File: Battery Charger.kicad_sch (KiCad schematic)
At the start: 2 parts, among them Q9 2SJ174, U16 CN3703

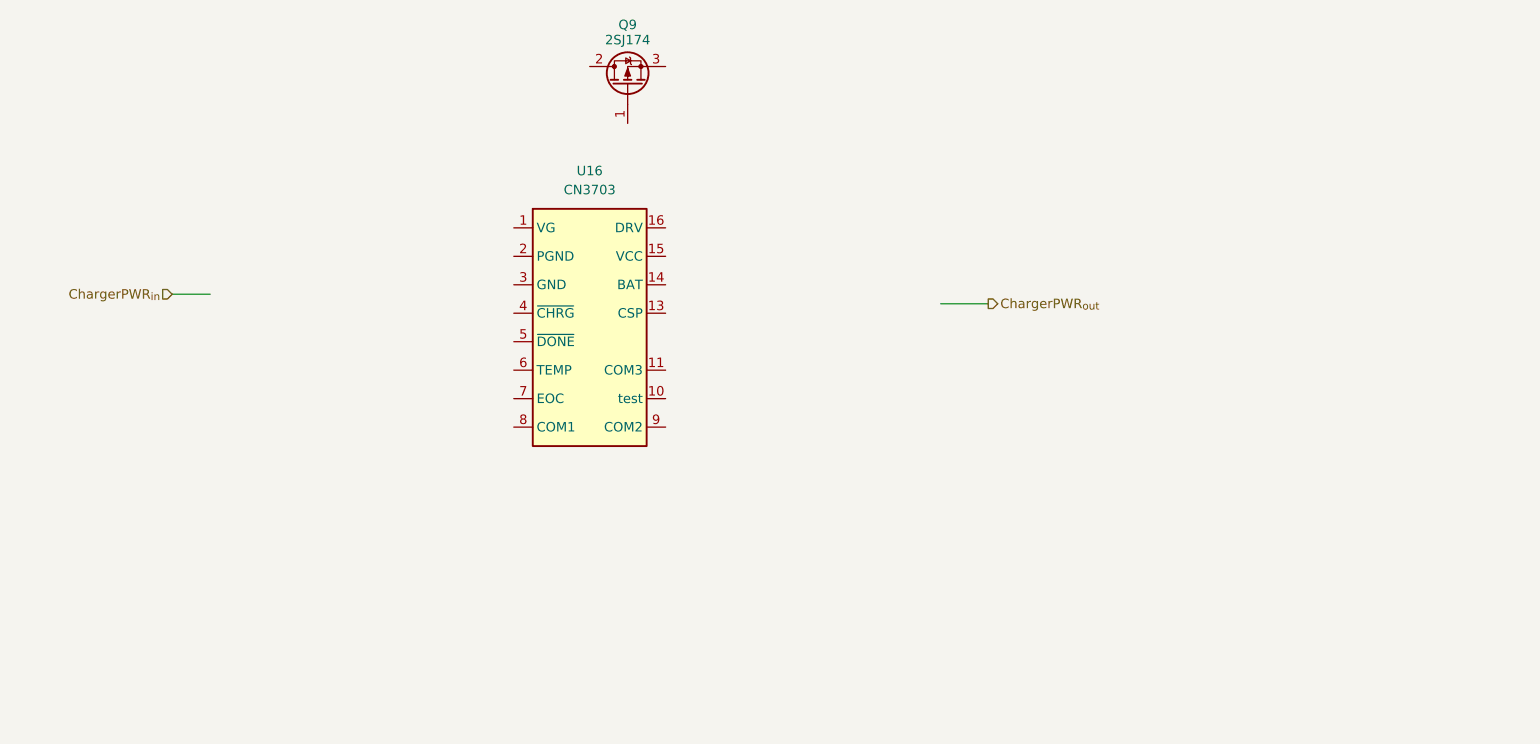
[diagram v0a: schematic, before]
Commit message: feat: Battery charging Circuit is added.
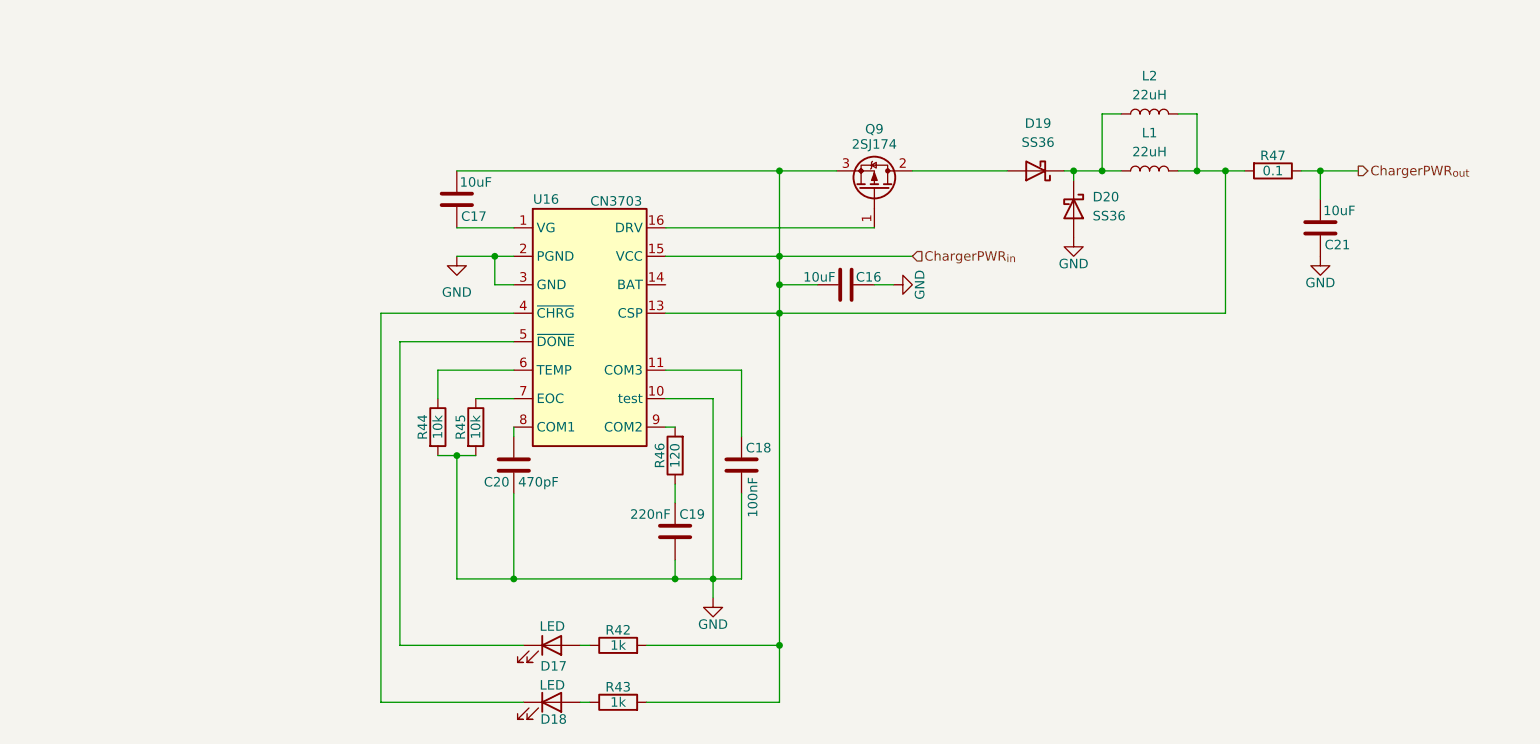
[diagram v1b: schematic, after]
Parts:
- added C16, C17, C21: 10uF, Capacitor_THT:C_Radial_D5.0mm_H5.0mm_P2.00mm, symbol Device:C
- added C18: 100nF, Capacitor_THT:C_Disc_D3.0mm_W2.0mm_P2.50mm, symbol Device:C
- added C19: 220nF, Capacitor_THT:C_Disc_D3.0mm_W2.0mm_P2.50mm, symbol Device:C
- added C20: 470pF, Capacitor_THT:C_Disc_D3.0mm_W2.0mm_P2.50mm, symbol Device:C
- added D17, D18: LED, LED_SMD:LED_1206_3216Metric, symbol Device:LED
- added D19, D20: SS36, Diode_SMD:D_SMA, symbol Diode:SS36
- added L1, L2: 22uH, Inductor_SMD:L_12x12mm_H4.5mm, symbol Device:L
- added R42, R43: 1k, Resistor_SMD:R_1206_3216Metric_Pad1.30x1.75mm_HandSolder, symbol Device:R
- added R44, R45: 10k, Resistor_SMD:R_1206_3216Metric_Pad1.30x1.75mm_HandSolder, symbol Device:R
- added R46: 120, Resistor_SMD:R_1206_3216Metric_Pad1.30x1.75mm_HandSolder, symbol Device:R
- added R47: 0.1, Resistor_SMD:R_2512_6332Metric_Pad1.40x3.35mm_HandSolder, symbol Device:R
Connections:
- net ChargerPWR_{in}: now also Q9.3 (S), U16.13 (CSP), U16.15 (VCC), C16.2, C17.2, L1.2, L2.2, R42.2, R43.2, R47.2
- net ChargerPWR_{out}: now also C21.2, R47.1
- net at Q9.1 (G): now also U16.16 (DRV)
- net at Q9.2 (D): now also D19.2 (A)
- net at U16.1 (VG): now also C17.1
- net GND: now reaches U16.10 (test)
- net GND: now also U16.2 (PGND), U16.3 (GND), C16.1, C18.1, C19.1, C20.1, C21.1, D20.2 (A), R44.2, R45.2
- net at U16.11 (COM3): now also C18.2
- net at U16.4 (~{CHRG}): now also D18.1 (K)
- net at U16.5 (~{DONE}): now also D17.1 (K)
- net at U16.6 (TEMP): now also R44.1
- net at U16.7 (EOC): now also R45.1
- net at U16.8 (COM1): now also C20.2
- net at U16.9 (COM2): now also R46.2
- new net: D19.1 (K), D20.1 (K), L1.1, L2.1
- new net: D18.2 (A), R43.1
- new net: C19.2, R46.1
- new net: D17.2 (A), R42.1
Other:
- moved on the sheet: Q9
